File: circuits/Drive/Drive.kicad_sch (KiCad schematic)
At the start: 23 parts, among them J1 Conn_01x14_Pin, SW1 SW_SPST, U1 STM32F446VETx, Y1 16MHz

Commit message: Driveほぼ完成
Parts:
- removed C10, C15: 0.1uF, Capacitor_SMD:C_0402_1005Metric, symbol Device:C
- removed C12, C13: 2.2uF, Capacitor_SMD:C_0402_1005Metric, symbol Device:C
- removed C14: 4.7uF, Capacitor_SMD:C_0603_1608Metric, symbol Device:C
- removed R3: 1k, Resistor_SMD:R_0402_1005Metric, symbol Device:R
- removed U1: STM32F446VETx, Package_QFP:LQFP-100_14x14mm_P0.5mm, symbol MCU_ST_STM32F4:STM32F446VETx
- removed Y1: 16MHz, Crystal:Crystal_SMD_3225-4Pin_3.2x2.5mm_HandSoldering, symbol Device:Crystal_GND24
- added R62: 1k, Resistor_SMD:R_0402_1005Metric, symbol Device:R
- added U2: STM32F446RETx, Package_QFP:LQFP-64_10x10mm_P0.5mm, symbol MCU_ST_STM32F4:STM32F446RETx
- added Y2: 16MHz, Crystal:Crystal_SMD_3225-4Pin_3.2x2.5mm, symbol Device:Crystal_GND24
- C11: value 1uF -> 4.7uF; footprint Capacitor_SMD:C_0402_1005Metric -> Capacitor_SMD:C_0603_1608Metric
- C9: value 0.1uF -> 1uF
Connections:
- net +3.3V: now also C9.2, U2.1 (VBAT), U2.13 (VDDA), U2.19 (VDD), U2.32 (VDD), U2.48 (VDD), U2.64 (VDD); no longer C11.1, C9.1
- net BOOT0: now also U2.60 (BOOT0)
- net GNDD: now also C9.1, R62.2, U2.12 (VSSA), U2.18 (VSS), U2.31 (VSS), U2.47 (VSS), U2.63 (VSS), Y2.2, Y2.4; no longer C9.2
- net HSE_IN: now also U2.5 (PH0), Y2.1
- net HSE_OUT: now also U2.6 (PH1), Y2.3
- net NRST: now also U2.7 (NRST)
- net SWCLK: now also U2.49 (PA14)
- net SWDIO: now also U2.46 (PA13)
- net SWO: now also U2.55 (PB3)
- net at R2.1: now also U2.28 (PB2)
- net VBUS: no longer names the net of D1.1 (K), J1.3 (Pin_3)
- net VBUS: now also R62.1
- new net: C11.1, U2.30 (VCAP_1)
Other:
- sheet RS485 renamed RS485_RingNW
- added sheet RS485_MD (RS485_MD.kicad_sch)
- sheet RS485_RingNW: file RS485.kicad_sch -> RS485_RingNW.kicad_sch
- sheet RS485_RingNW ports: added MainRX_RS485RingX_TX, MainRX_RS485RingY_TX, MainTX_RS485RingX_RX, MainTX_RS485RingY_RX; removed MainRX_RS485Bst_TX, MainRX_RS485Cam_TX, MainRX_RS485MD_TX, MainRX_RS485Spr_TX, MainRX_RS485UI_TX, MainTX_RS485Bst_RX, MainTX_RS485Cam_RX, MainTX_RS485MD_RX, MainTX_RS485Spr_RX, MainTX_RS485UI_RX
- sheet UI ports: added DIP_SW0, DIP_SW1, DIP_SW2, DIP_SW3; removed Slide_SW1, Tact_SW0
- note added: "F446RE"
- note removed: "F446VE"
- moved on the sheet: C1, C2, C3, C4, C5, C6, C7, R1, R2, SW1

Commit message: 無線&UI完成？
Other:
- sheet BNO055 ports: added BNO_INT; removed none

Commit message: ラズパイ基板とか
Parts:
- added Q15, Q16: BSS138, Package_TO_SOT_SMD:SOT-23, symbol Device:Q_NMOS_GSD
- added R3, R59: 10k, Resistor_SMD:R_0402_1005Metric, symbol Device:R
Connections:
- net GNDD: now also Q15.2 (S), Q16.2 (S), R3.2, R59.2
- new net INT_Mouse: Q16.3 (D)
- new net Main->INT_Mouse: Q16.1 (G), R59.1
- new net Main->RST_BNO: Q15.1 (G), R3.1
- new net RST_BNO: Q15.3 (D)
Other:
- sheet BNO055 ports: added INT, nRST; removed BNO_INT, BNO_RST
- sheet Mouse ports: added INT; removed Mouse_INT
- sheet UI ports: added DIPSW0, DIPSW1, DIPSW2, DIPSW3, SlideSW0; removed DIP_SW0, DIP_SW1, DIP_SW2, DIP_SW3, Slide_SW0
- note added: "Main to BNO055 Reset"
- note added: "Main to PIM573 Initialize"

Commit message: PDFプロット
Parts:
- added C10: 0.1uF, Capacitor_SMD:C_0402_1005Metric, symbol Device:C
- added R68: 10k, Resistor_SMD:R_0402_1005Metric, symbol Device:R
- added SW5: SW_SPST, symbol Switch:SW_SPST
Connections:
- net +3.3V: now also C10.1, SW5.2 (B)
- net GNDD: now also R68.2
- new net SHDN/BOOT: C10.2, R68.1, SW5.1 (A)
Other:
- sheet UI ports: added LED_B0, LED_B1, LED_LG0, LED_Y0, LED_nR0; removed LED0, LED1
- note added: "ShutDown/BOOT Switch"
- moved on the sheet: C1, C11, C2, C3, C4, C5, C6, C7, C9, D1, J1, Q15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

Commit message: シンボル・フットプリントMyLib->TomoshibiLib置き換え
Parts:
- J1: footprint MyLibrary:BoxHeader_2x07_P1.27mm_Horizontal -> TomoshibiLibrary:BoxHeader_2x07_P1.27mm_Horizontal
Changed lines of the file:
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@@
       (effects (font (size 1.27 1.27)))
     )
-    (property "Footprint" "MyLibrary:BoxHeader_2x07_P1.27mm_Horizontal" (at 38.1 134.62 0)
+    (property "Footprint" "TomoshibiLibrary:BoxHeader_2x07_P1.27mm_Horizontal" (at 38.1 134.62 0)
       (effects (font (size 1.27 1.27)) hide)
     )

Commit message: 更新
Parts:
- removed C11: 4.7uF, Capacitor_SMD:C_0603_1608Metric, symbol Device:C
- removed Q15, Q16: BSS138, Package_TO_SOT_SMD:SOT-23, symbol Device:Q_NMOS_GSD
- removed R2: 10k, Resistor_SMD:R_0402_1005Metric, symbol Device:R
- removed U2: STM32F446RETx, Package_QFP:LQFP-64_10x10mm_P0.5mm, symbol MCU_ST_STM32F4:STM32F446RETx
- added C12: 4.7uF, Capacitor_SMD:C_0603_1608Metric, symbol Device:C
- added C13: 1uF, Capacitor_SMD:C_0402_1005Metric, symbol Device:C
- added C14, C15: 2.2uF, Capacitor_SMD:C_0402_1005Metric, symbol Device:C
- added Q15, Q16: 2N7002, Package_TO_SOT_SMD:SOT-23, symbol Transistor_FET:2N7002
- added U8: STM32H723VGTx, Package_QFP:LQFP-100_14x14mm_P0.5mm, symbol MCU_ST_STM32H7:STM32H723VGTx
- C9: value 1uF -> 0.1uF
- SW5: footprint (none) -> Button_Switch_THT:SW_PUSH_1P1T_6x3.5mm_H4.3_APEM_MJTP1243
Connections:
- net +3.3V: now also C9.1, C12.1, C13.1, U8.100 (VDD), U8.11 (VDD), U8.20 (VREF+), U8.21 (VDDA), U8.27 (VDD), U8.50 (VDD), U8.6 (VBAT), U8.75 (VDD); no longer C9.2
- net BOOT0: now also U8.94 (BOOT0)
- net CSx_Mouse: now also U8.51 (PB12)
- net DIPSW0: now also U8.64 (PC7)
- net DIPSW1: now also U8.65 (PC8)
- net DIPSW2: now also U8.66 (PC9)
- net DIPSW3: now also U8.67 (PA8)
- net GNDD: now also C9.2, C12.2, C13.2, C14.2, C15.2, Q15.2 (S), Q16.2 (S), U8.10 (VSS), U8.19 (VSSA), U8.26 (VSS), U8.49 (VSS), U8.74 (VSS), U8.99 (VSS); no longer C9.1
- net HSE_IN: now also U8.12 (PH0)
- net HSE_OUT: now also U8.13 (PH1)
- net INT_BNO: now also U8.57 (PD10)
- net INT_Mouse: now also Q15.3 (D)
- net LED_B0: now also U8.87 (PD6)
- net LED_B1: now also U8.78 (PC10)
- net LED_LG0: now also U8.92 (PB6)
- net LED_Y0: now also U8.93 (PB7)
- net LED_nR0: now also U8.83 (PD2)
- net MISOx: now also U8.53 (PB14)
- net MOSIx: now also U8.54 (PB15)
- net Main->INT_Mouse: now also Q15.1 (G), U8.55 (PD8)
- net Main->RST_BNO: now also Q16.1 (G), U8.62 (PD15)
- net MainRXx_RS485MDTX: now also U8.25 (PA3)
- net MainRXx_RS485RingXTX: now also U8.69 (PA10)
- net MainRXx_RS485RingYTX: now also U8.70 (PA11)
- net MainTXx_RS485MDRX: now also U8.24 (PA2)
- net MainTXx_RS485RingXRX: now also U8.68 (PA9)
- net MainTXx_RS485RingYRX: now also U8.71 (PA12)
- net NRST: now also U8.14 (NRST)
- net RST_BNO: now also Q16.3 (D)
- net SCLKx: now also U8.52 (PB13)
- net SCLx: now also U8.59 (PD12)
- net SDAx: now also U8.60 (PD13)
- net SHDN/BOOT: now also U8.61 (PD14)
- net SWCLK: now also U8.76 (PA14(JTCK)
- net SWDIO: now also U8.72 (PA13(JTMS)
- net SWO: now also U8.89 (PB3(JTDO)
- net SlideSW0: now also U8.63 (PC6)
- net V_Meas.: now also U8.23 (PA1)
- new net: C14.1, U8.48 (VCAP)
- new net: C15.1, U8.73 (VCAP)
- no-connect marks 11 -> 56
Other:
- moved on the sheet: C1, C2, C3, C4, C5, C6, C7, D1, J1, R1, R62, SW1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

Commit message: raspi基板回路図
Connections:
- net CSx_Mouse renamed CS2_Mouse
- net MISOx renamed MISO2
- net MOSIx renamed MOSI2
- net MainRXx_RS485MDTX renamed MainRX2_RS485MDTX
- net MainRXx_RS485RingXTX renamed MainRX1_RS485RingXTX
- net MainRXx_RS485RingYTX renamed MainRX4_RS485RingYTX
- net MainTXx_RS485MDRX renamed MainTX2_RS485MDRX
- net MainTXx_RS485RingXRX renamed MainTX1_RS485RingXRX
- net MainTXx_RS485RingYRX renamed MainTX4_RS485RingYRX
- net SCLKx renamed SCLK2
- net SCLx renamed SCL4
- net SDAx renamed SDA4
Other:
- note added: "H723VG"
- note removed: "F446RE"

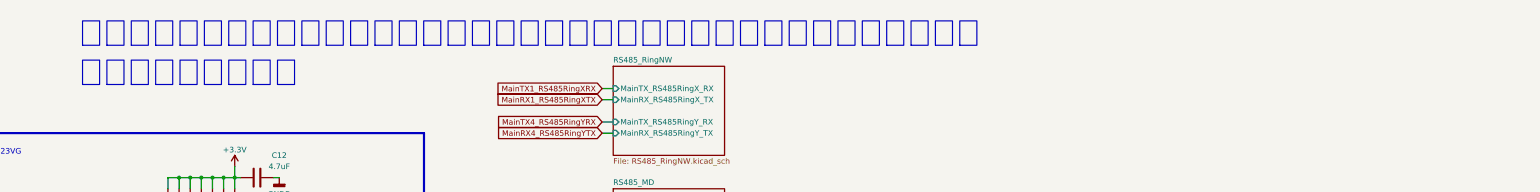
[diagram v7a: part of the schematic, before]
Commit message: 発注_第一弾
Drive, 1stLayer_Power, 2ndLayer_3rdLayer
を発注
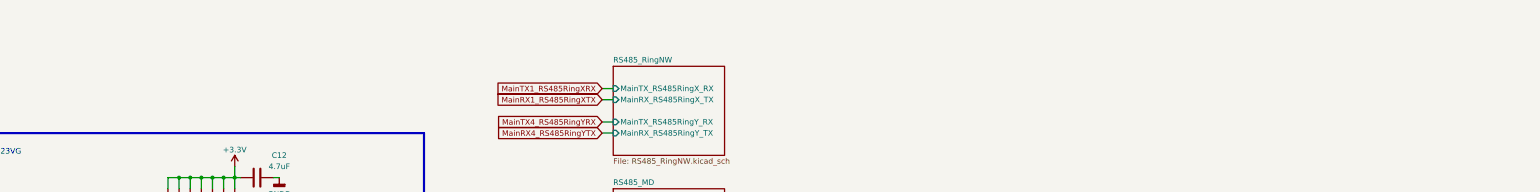
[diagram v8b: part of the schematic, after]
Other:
- note removed: "マイコン側のラベルと階層シート側のラベルをそれぞれ対応するように書き換える 電解コンの耐圧注意"
